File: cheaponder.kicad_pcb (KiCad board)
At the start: 2 copper layers, 18 x 22.5 mm, 32 parts, among them J1 B+, J2 B-, Q1 FS8205A, U1 TP4057, U2 DW01A, U3 TPS63900, U4 ESP32-S3-Zero Devboard

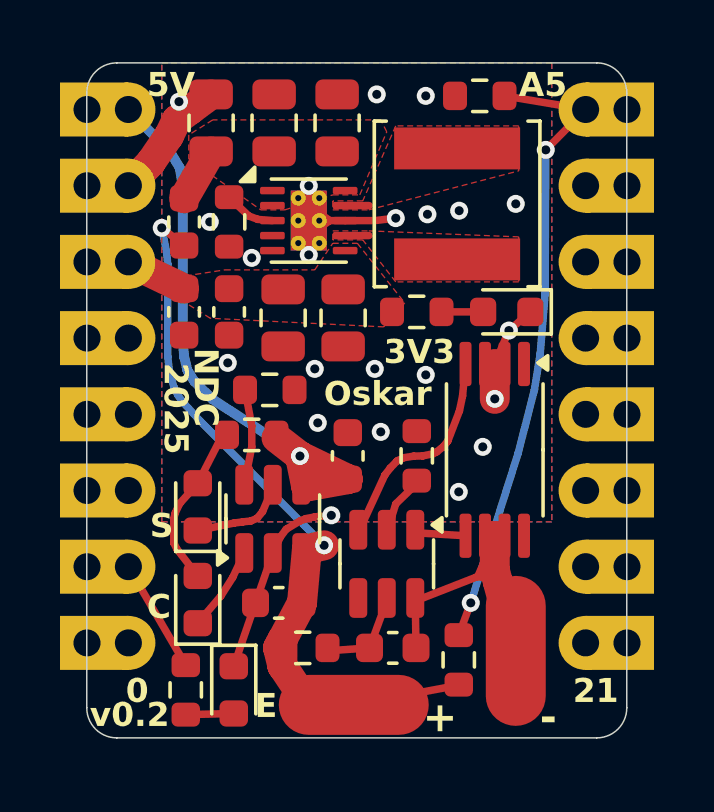
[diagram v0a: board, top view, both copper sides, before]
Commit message: Relayout to accomodate bigger cap and put LEDs where we can see them
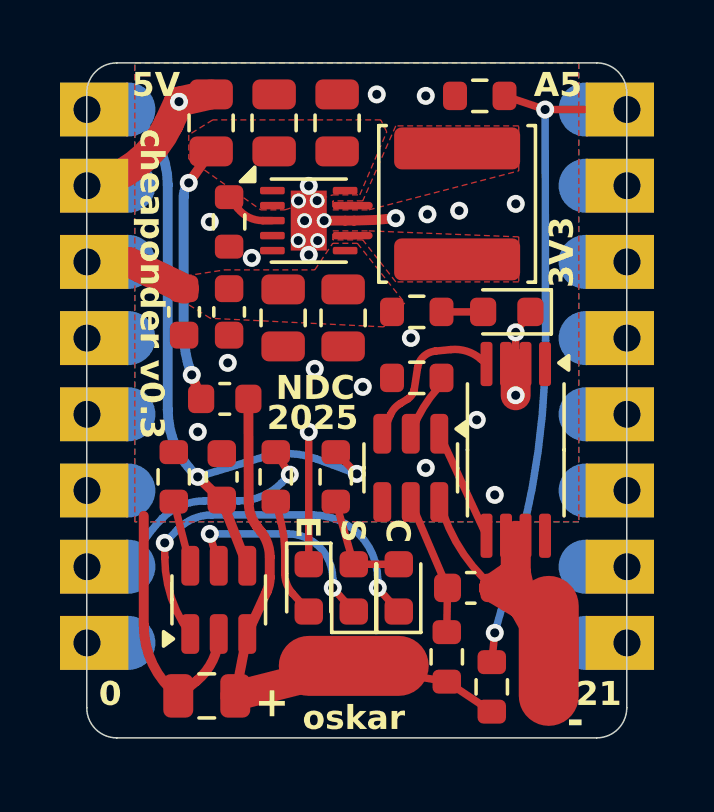
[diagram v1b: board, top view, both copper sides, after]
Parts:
- added G***: LOGO, LOGO, F.Cu at (86.9, 115.9)
- C3: footprint Capacitor_SMD:C_0603_1608Metric -> Capacitor_SMD:C_0805_2012Metric
- U3: footprint Package_SON:WSON-10-1EP_2.5x2.5mm_P0.5mm_EP1.2x2mm_ThermalVias -> Package_SON:WSON-10-1EP_2.5x2.5mm_P0.5mm_EP1.2x2mm
- moved R7 7.71 mm to (78.9, 116.8)
- moved D2 6.71 mm to (83.0, 120.5)
- moved F1 6.05 mm to (77.2, 114.2), turned to 180 degrees
- moved D1 5.86 mm to (81.5, 120.5)
- moved R2 4.81 mm to (84.6, 122.8), turned to -90 degrees
- moved R3 4.32 mm to (75.5, 116.8), turned to -90 degrees
- moved C2 4.26 mm to (77.1, 116.8)
- moved D4 4.22 mm to (80.0, 120.5)
- moved C3 3.92 mm to (76.6, 124.1)
- moved U2 3.30 mm to (83.4, 116.5)
- moved C1 3.28 mm to (85.4, 120.5)
- moved U1 3.24 mm to (77.0, 120.9)
- moved R1 3.13 mm to (80.9, 116.8), turned to 90 degrees
- moved R4 2.60 mm to (83.6, 113.5), turned to 0 degrees
- moved R8 1.42 mm to (86.1, 123.8)
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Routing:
- net /TP_CHRG: track 2.82 -> 13.1 mm, vias 0 -> 2
- net /+VIN: track 1.80 -> 8.61 mm, vias 0 -> 2
- net +BATT: track 25.8 -> 19.3 mm, vias 2 -> 0
- net GND: track 19.8 -> 24.2 mm, vias 22 -> 28
- net /TP_STBY: track 3.18 -> 7.35 mm, vias 0 -> 2
- net /ESP_LED: track 3.80 -> 7.52 mm, vias 0 -> 1
- net VBUS: track 19.3 -> 22.9 mm, vias 1 -> 2
- net Net-(D4-A): track 1.60 -> 3.96 mm
- net /DW_OD: track 1.68 -> 3.75 mm
- net /DW_OC: track 7.29 -> 5.31 mm
- net Net-(D1-A): track 5.32 -> 3.67 mm
- net /VBAT_MON: track 21.2 -> 22.8 mm
- net Net-(U2-VCC): track 3.07 -> 4.59 mm
- net -BATT: track 11.2 -> 10.2 mm
- net Net-(U1-PROG): track 3.21 -> 2.21 mm
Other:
- board text added: "cheaponder v0.3"
- board text added: "oskar"
- board text removed: "Oskar"
- board text removed: "v0.2"

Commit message: Add comment and fix trace distance
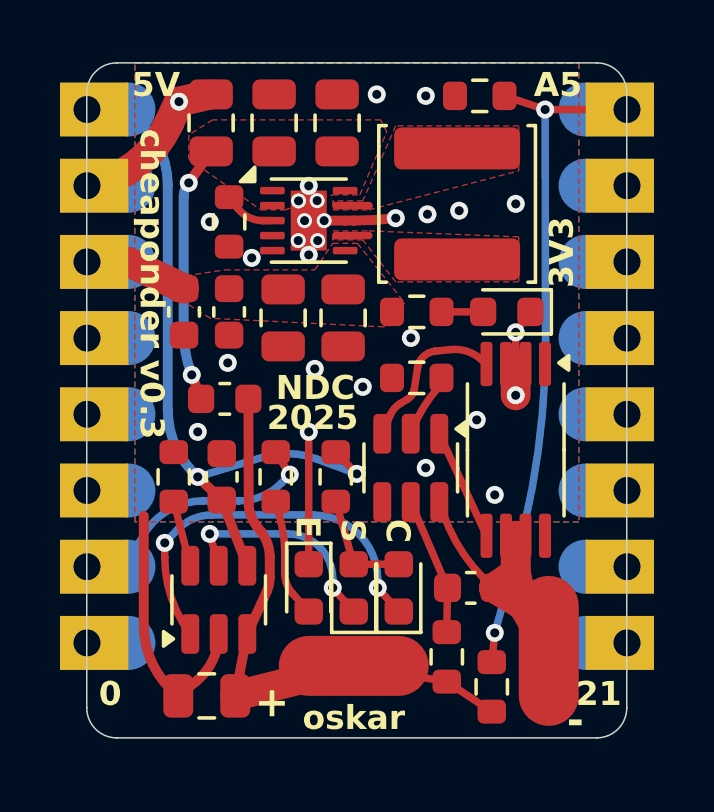
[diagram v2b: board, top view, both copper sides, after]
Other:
- board text added: "Decided against plated slots for the BAT wires because a) space on the backside of -BATT is limited and b) i don't want any metal too near to the ESP32 antenna"
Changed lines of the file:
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@@
+		)
+	)
+	(gr_text "Decided against plated slots for the BAT wires because\na) space on the backside of -BATT is limited and\nb) i don't want any metal too near to the ESP32 antenna"
+		(at 79.4 126.8 0)
+		(layer "User.4")
+		(effects
+			(font
+				(size 0.2 0.2)
+				(thickness 0.05)
+				(bold yes)
+			)
+			(justify left bottom)
 		)
 	)
@@
 	)
 	(segment
-		(start 75.113454 118.186546)
-		(end 75.111756 118.188244)
+		(start 73.988 119.794)
+		(end 74.377701 118.949136)
 		(width 0.25)
 		(layer "B.Cu")
@@
 	(segment
 		(start 77.660264 117.6)
-		(end 76.529502 117.6)
+		(end 76.485741 117.6)
 		(width 0.25)
 		(layer "B.Cu")
 		(net 19)
 	)
-	(segment
-		(start 74.401758 119.100141)
-		(end 73.988 119.794)
+	(arc
+		(start 79.091931 117.004375)
+		(mid 78.435577 117.445154)
+		(end 77.660264 117.6)
 		(width 0.25)
 		(layer "B.Cu")
@@
 	)
 	(arc
-		(start 74.401758 119.100141)
-		(mid 74.728487 118.622182)
-		(end 75.111756 118.188244)
-		(width 0.25)
-		(layer "B.Cu")
-		(net 19)
-	)
-	(arc
-		(start 77.660264 117.6)
-		(mid 78.435577 117.445154)
-		(end 79.091931 117.004375)
-		(width 0.25)
-		(layer "B.Cu")
-		(net 19)
-	)
-	(arc
-		(start 75.113454 118.186546)
-		(mid 75.763142 117.752438)
-		(end 76.529502 117.6)
-		(width 0.25)
-		(layer "B.Cu")
+		(start 74.377701 118.949136)
+		(mid 75.234342 117.966161)
+		(end 76.485741 117.6)
+		(width 0.25)
+		(layer "B.Cu")
